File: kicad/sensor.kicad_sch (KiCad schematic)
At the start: 6 parts

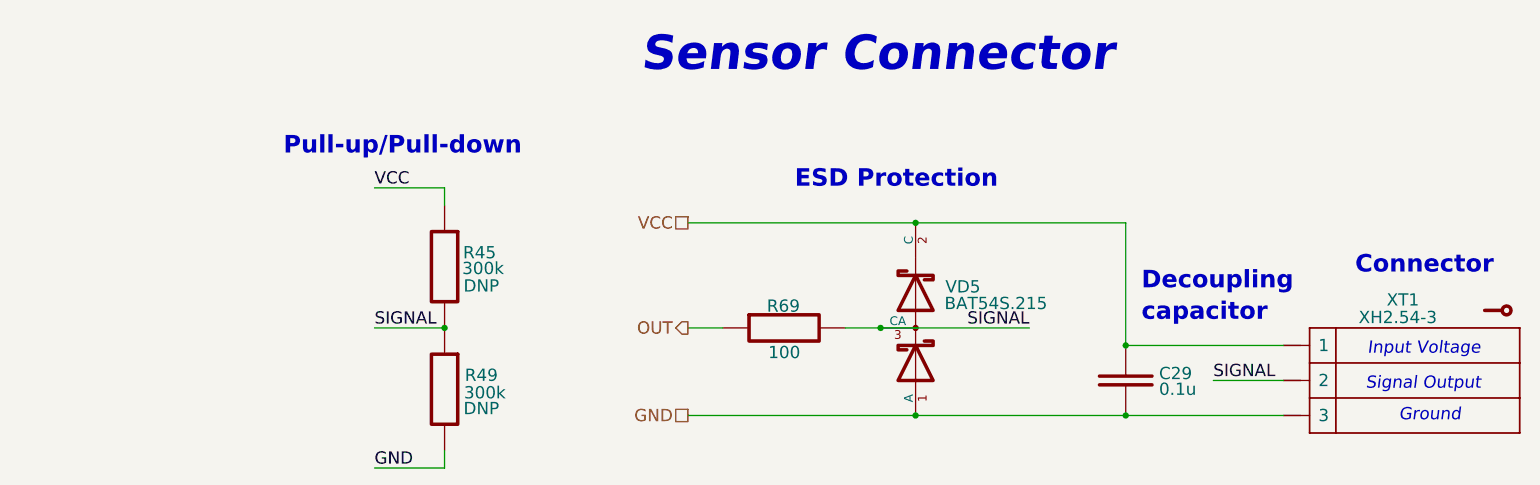
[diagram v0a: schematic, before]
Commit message: Reannotate schematic; Fix 5032 crystal footprint field; Update PCB with 5032 crystal
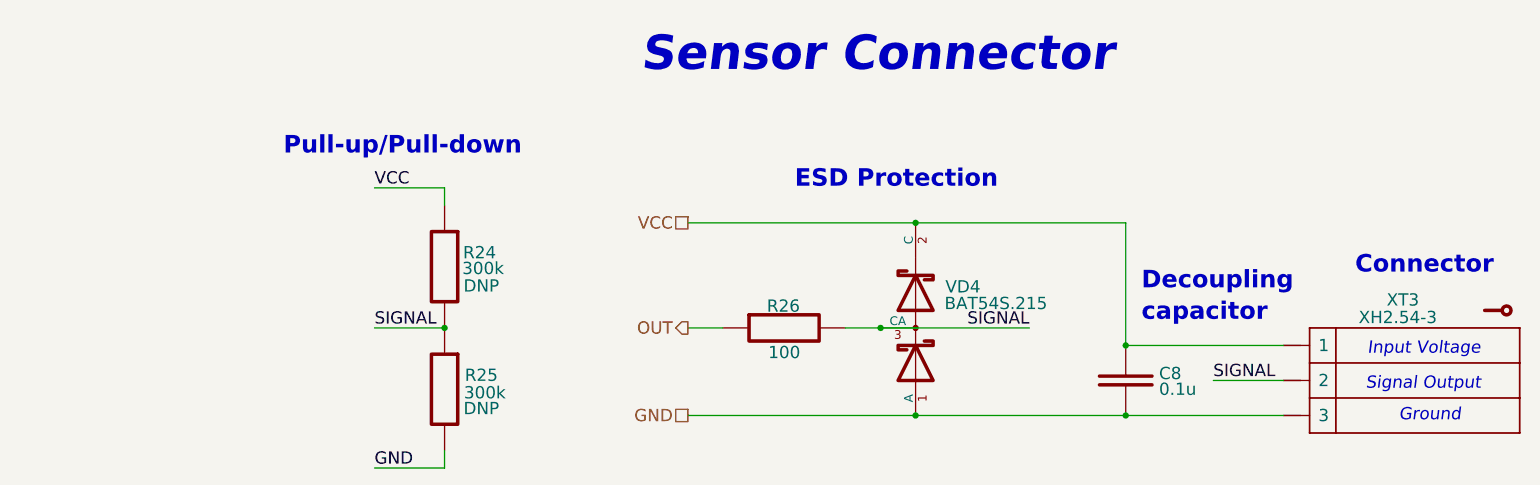
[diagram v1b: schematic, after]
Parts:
- renumbered C29 to C8, R45 to R24, R49 to R25, R69 to R26, VD5 to VD4, XT1 to XT3
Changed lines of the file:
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@@
   (symbol (lib_id "Connectors:XT_CONTACT_ARR3") (at 242.316 109.728 0) (unit 1)
     (in_bom yes) (on_board yes)
-    (property "Reference" "XT1" (id 0) (at 239.522 98.044 0)
+    (property "Reference" "XT3" (id 0) (at 239.522 98.044 0)
       (effects (font (size 1.778 1.778)) (justify left))
     )
@@
   (symbol (lib_id "Capacitors:C_CAP") (at 201.676 109.728 270) (unit 1)
     (in_bom yes) (on_board yes)
-    (property "Reference" "C29" (id 0) (at 206.502 108.7121 90)
+    (property "Reference" "C8" (id 0) (at 206.502 108.7121 90)
       (effects (font (size 1.778 1.778)) (justify left))
     )
@@
   (symbol (lib_id "Resistors:R_RES") (at 152.1183 102.108 0) (unit 1)
     (in_bom yes) (on_board yes)
-    (property "Reference" "R69" (id 0) (at 152.019 98.933 0)
+    (property "Reference" "R26" (id 0) (at 152.019 98.933 0)
       (effects (font (size 1.778 1.778)))
     )
@@
   (symbol (lib_id "Resistors:R_RES") (at 102.87 110.998 270) (unit 1)
     (in_bom yes) (on_board yes)
-    (property "Reference" "R49" (id 0) (at 108.204 108.966 90)
+    (property "Reference" "R25" (id 0) (at 108.204 108.966 90)
       (effects (font (size 1.778 1.778)))
     )
@@
   (symbol (lib_id "Resistors:R_RES") (at 102.87 93.218 270) (unit 1)
     (in_bom yes) (on_board yes)
-    (property "Reference" "R45" (id 0) (at 107.95 91.186 90)
+    (property "Reference" "R24" (id 0) (at 107.95 91.186 90)
       (effects (font (size 1.778 1.778)))
     )
@@
   (symbol (lib_id "Diodes:VD_SCHOTTKY_PROTECT") (at 171.196 102.108 0) (unit 1)
     (in_bom yes) (on_board yes)
-    (property "Reference" "VD5" (id 0) (at 175.514 96.139 0)
+    (property "Reference" "VD4" (id 0) (at 175.514 96.139 0)
       (effects (font (size 1.778 1.778)) (justify left))
     )

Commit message: Add voltage value to caps, update BOM, SCH, ASM
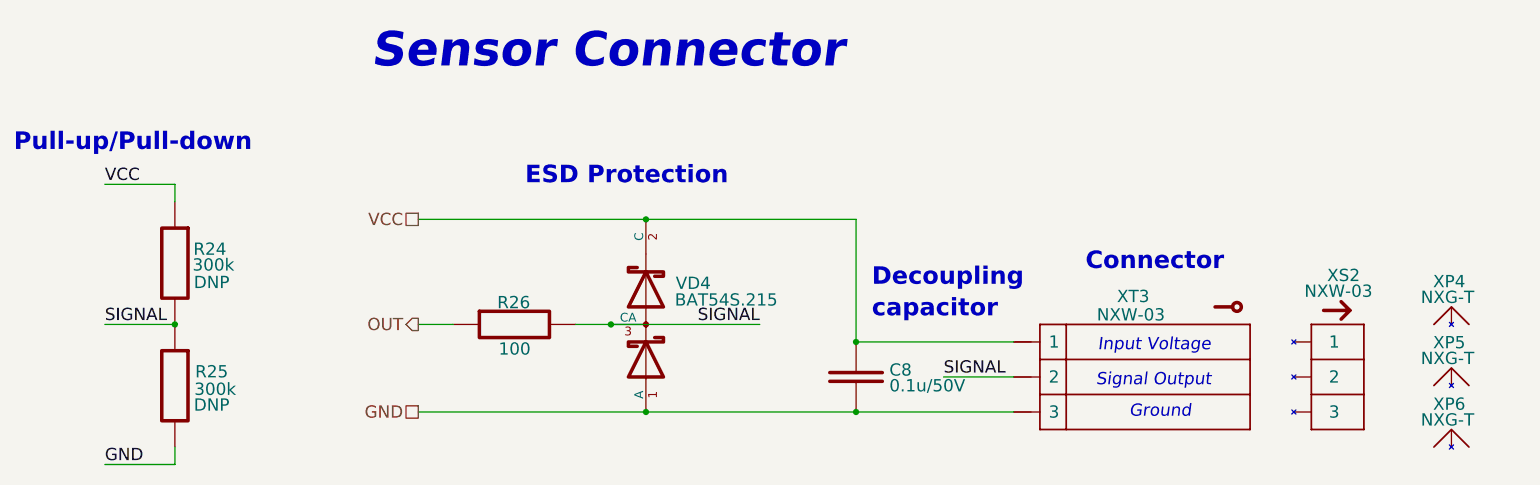
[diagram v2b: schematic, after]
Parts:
- added XP4, XP5, XP6: NXG-T, symbol Connectors:XS_TERMINAL
- added XS2: NXW-03, symbol Connectors:XS_PLUG3
- C8: value 0.1u -> 0.1u/50V; Tolerance (none) -> ±10%; Type (none) -> X7R
- R24, R25, R26: Case/Package 0000 -> 0603; Tolerance ±% -> ±5%
- XT3: value XH2.54-3 -> NXW-03
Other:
- moved on the sheet: C8, R24, R25, R26, VD4, XT3

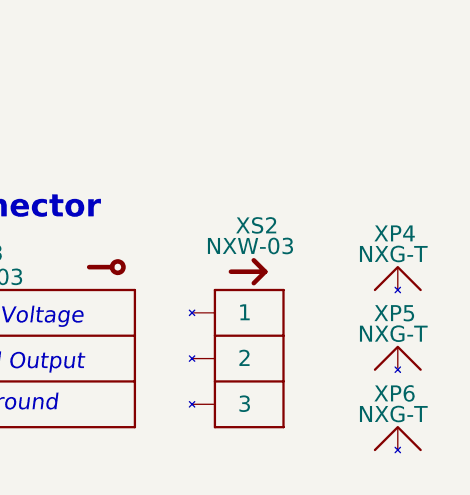
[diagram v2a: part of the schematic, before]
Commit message: Add docs; Update values of components according to PCB
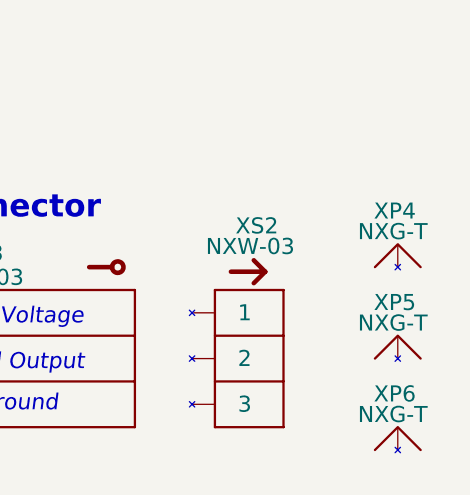
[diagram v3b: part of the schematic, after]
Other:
- moved on the sheet: XP4, XP5
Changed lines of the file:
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@@
     (pin "3")
   )
-  (symbol (lib_id "Connectors:XS_TERMINAL") (at 248.92 101.6 0) (unit 1)
+  (symbol (lib_id "Connectors:XS_TERMINAL") (at 248.92 99.06 0) (unit 1)
     (in_bom yes) (on_board no)
-    (property "Reference" "XP4" (id 0) (at 246.253 95.377 0)
+    (property "Reference" "XP4" (id 0) (at 246.253 92.837 0)
       (effects (font (size 1.778 1.778)) (justify left))
     )
-    (property "Value" "NXG-T" (id 1) (at 244.475 97.663 0)
+    (property "Value" "NXG-T" (id 1) (at 244.475 95.123 0)
       (effects (font (size 1.778 1.778)) (justify left))
     )
-    (property "Footprint" "" (id 2) (at 248.92 101.6 0)
+    (property "Footprint" "" (id 2) (at 248.92 99.06 0)
       (effects (font (size 1.778 1.778)) hide)
     )
-    (property "Datasheet" "" (id 3) (at 248.92 101.6 0)
+    (property "Datasheet" "" (id 3) (at 248.92 99.06 0)
       (effects (font (size 1.778 1.778)) hide)
     )
@@
     (pin "2")
   )
-  (symbol (lib_id "Connectors:XS_TERMINAL") (at 248.92 110.4584 0) (unit 1)
+  (symbol (lib_id "Connectors:XS_TERMINAL") (at 248.92 109.22 0) (unit 1)
     (in_bom yes) (on_board no)
-    (property "Reference" "XP5" (id 0) (at 246.253 104.2354 0)
+    (property "Reference" "XP5" (id 0) (at 246.253 102.997 0)
       (effects (font (size 1.778 1.778)) (justify left))
     )
-    (property "Value" "NXG-T" (id 1) (at 244.475 106.5214 0)
+    (property "Value" "NXG-T" (id 1) (at 244.475 105.283 0)
       (effects (font (size 1.778 1.778)) (justify left))
     )
-    (property "Footprint" "" (id 2) (at 248.92 110.4584 0)
+    (property "Footprint" "" (id 2) (at 248.92 109.22 0)
       (effects (font (size 1.778 1.778)) hide)
     )
-    (property "Datasheet" "" (id 3) (at 248.92 110.4584 0)
+    (property "Datasheet" "" (id 3) (at 248.92 109.22 0)
       (effects (font (size 1.778 1.778)) hide)
     )

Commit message: Add wiring diagram; Add work ours (stage 2); refactor folders
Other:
- title: (none) -> RadioSens v1
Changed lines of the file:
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@@
 (kicad_sch (version 20211123) (generator eeschema)
   (paper "A4")
+  (title_block
+    (title "RadioSens v1")
+    (comment 2 "Electrical Circuit")
+  )
   (junction (at 162.56 114.3) (diameter 0) (color 0 0 0 0)
   )
